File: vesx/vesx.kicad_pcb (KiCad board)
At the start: 4 copper layers, 100 x 40 mm, 181 parts, among them J1 TYPE-C-31-M-12, J2 Conn_01x05, J3 Conn_01x06, J4 Conn_01x03, J5 Conn_01x04, J6 STLINK, J8 CAN, U1 Opamp_Quad, U2 LM1117DT-3.3, U3 LM5164DDA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

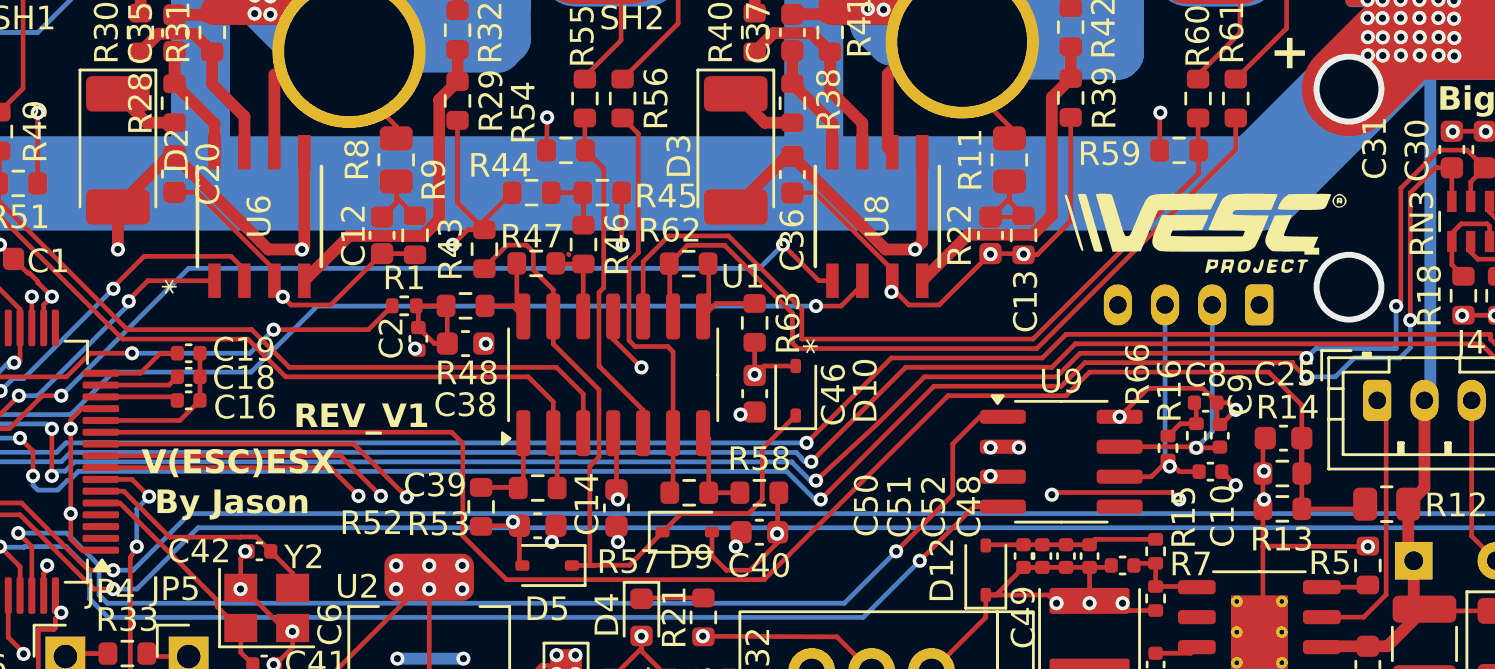
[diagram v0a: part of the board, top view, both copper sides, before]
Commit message: vesc logo del
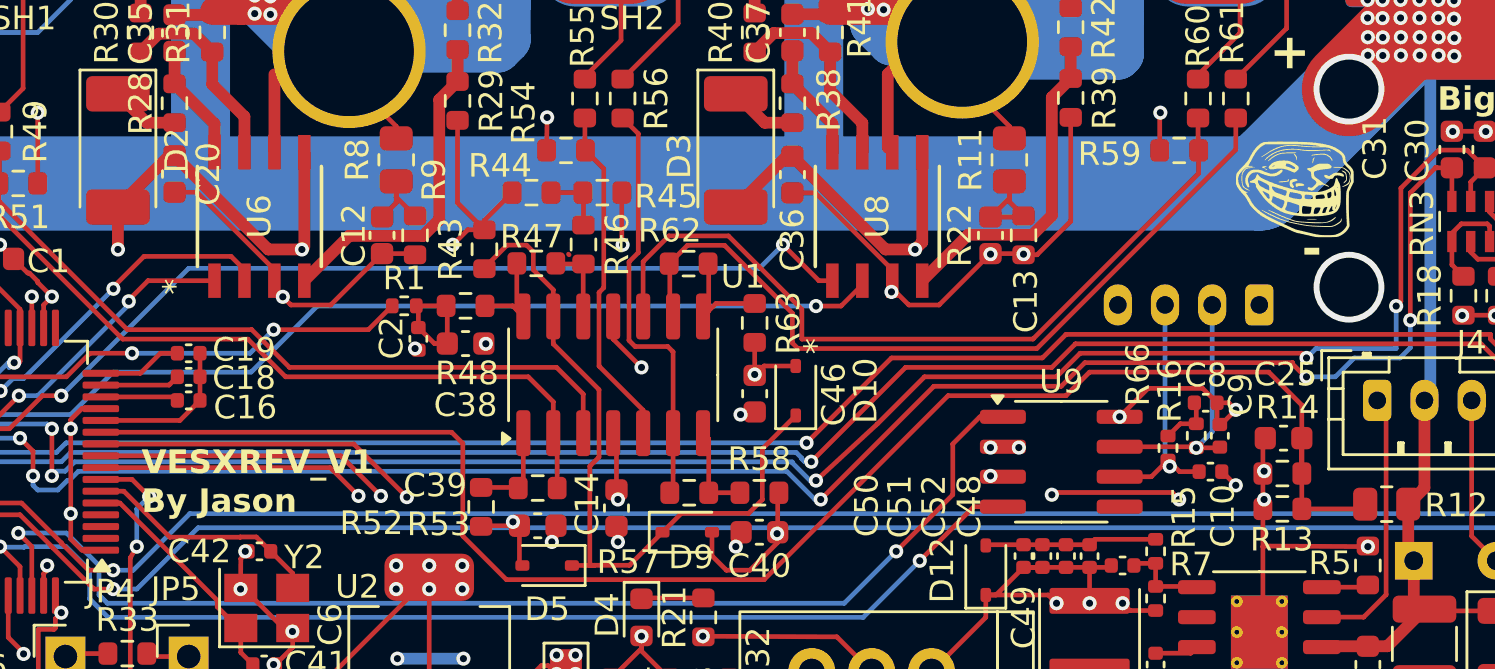
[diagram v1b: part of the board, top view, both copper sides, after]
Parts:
- moved G*** 4.23 mm to (235.7, 28.9)
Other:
- board text added: "VESX"
- board text removed: "V(ESC)ESX"

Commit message: asdf
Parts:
- removed the G*** at (235.7, 28.9)

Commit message: aaaaaaaaaaaaaaaaaaaaaaaaaaaaaaaaaaaaaaaa
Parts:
- C1: footprint Capacitor_SMD:C_0603_1608Metric -> Capacitor_SMD:C_0402_1005Metric
- C24: value 100nF -> 1nF
- C38: value C_Small -> 10nF
- C43: footprint Capacitor_SMD:C_1210_3225Metric -> Capacitor_SMD:C_0603_1608Metric
- L1: footprint Inductor_SMD:L_Abracon_ASPI-4030S -> Inductor_SMD:L_TracoPower_TCK-047_5.2x5.8mm
- R15: footprint Resistor_SMD:R_0402_1005Metric -> Resistor_SMD:R_0603_1608Metric
- moved L1 1.51 mm to (225.5, 47.9)
- moved C43 1.12 mm to (240.5, 49.0)
- moved U4 0.72 mm to (222.1, 51.8)
- moved C1 0.45 mm to (181.0, 32.0)
- moved R15 0.28 mm to (230.0, 44.0)
- renumbered UART2 to J7
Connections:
- net PB11 renamed PB10
- C39 pad 1: CURRENT_A -> CURRENT_C
- C40 pad 1: CURRENT_A -> CURRENT_C
- C46 pad 1: CURRENT_A -> CURRENT_C
- D10 pad 2: CURRENT_A -> CURRENT_C
- D5 pad 2: CURRENT_A -> CURRENT_C
- D9 pad 2: CURRENT_A -> CURRENT_C
- R52 pad 2: CURRENT_A -> CURRENT_C
- R58 pad 2: CURRENT_A -> CURRENT_C
- R63 pad 2: CURRENT_A -> CURRENT_C
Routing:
- net VBAT: track 196.2 -> 197.0 mm
- net GND: track 421.4 -> 421.8 mm, vias 335 -> 333

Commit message: fix trace$ground plane
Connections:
- C39 pad 1: CURRENT_C -> CURRENT_A
- C40 pad 1: CURRENT_C -> CURRENT_B
- D5 pad 2: CURRENT_C -> CURRENT_A
- D9 pad 2: CURRENT_C -> CURRENT_B
- R52 pad 2: CURRENT_C -> CURRENT_A
- R58 pad 2: CURRENT_C -> CURRENT_B
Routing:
- net +3V3: track 378.0 -> 383.4 mm
- net GND: track 421.8 -> 425.4 mm
- net CURRENT_B: track 37.9 -> 37.2 mm

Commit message: eeeeeeeeeeeeeeeeeeee
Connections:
- C39 pad 1: CURRENT_A -> CURRENT_B
- C40 pad 1: CURRENT_B -> CURRENT_C
- D5 pad 2: CURRENT_A -> CURRENT_C
- R52 pad 2: CURRENT_A -> CURRENT_B
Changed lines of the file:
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@@
 			(layers "F.Cu" "F.Paste" "F.Mask")
 			(roundrect_rratio 0.25)
-			(net 48 "CURRENT_B")
+			(net 41 "CURRENT_C")
 			(pintype "passive")
 		)
@@
 			(layers "F.Cu" "F.Paste" "F.Mask")
 			(roundrect_rratio 0.25)
-			(net 34 "CURRENT_A")
+			(net 41 "CURRENT_C")
 			(pinfunction "A")
 			(pintype "passive")
@@
 			(layers "F.Cu" "F.Paste" "F.Mask")
 			(roundrect_rratio 0.25)
-			(net 34 "CURRENT_A")
+			(net 48 "CURRENT_B")
 			(pintype "passive")
 		)
@@
 			(layers "F.Cu" "F.Paste" "F.Mask")
 			(roundrect_rratio 0.25)
-			(net 34 "CURRENT_A")
+			(net 48 "CURRENT_B")
 			(pintype "passive")
 		)
@@
 	)
 	(segment
-		(start 197.925 41.775)
-		(end 195.8 39.65)
+		(start 195.8 39.65)
+		(end 185.075 39.65)
 		(width 0.2)
 		(layer "F.Cu")
@@
 	)
 	(segment
-		(start 213.2 36.34)
-		(end 212.8 36.74)
+		(start 198.05 41.9)
+		(end 195.8 39.65)
 		(width 0.2)
 		(layer "F.Cu")
@@
 	)
 	(segment
-		(start 195.8 39.65)
-		(end 185.075 39.65)
+		(start 213.2 36.34)
+		(end 212.8 36.74)
 		(width 0.2)
 		(layer "F.Cu")
@@
 	)
 	(via
-		(at 197.925 41.775)
+		(at 198.05 41.9)
 		(size 0.6)
 		(drill 0.3)
@@
 	)
 	(segment
-		(start 197.925 41.775)
-		(end 202.7 37)
+		(start 198.05 41.9)
+		(end 202.95 37)
 		(width 0.2)
 		(layer "In2.Cu")
@@
 	)
 	(segment
-		(start 202.7 37)
+		(start 202.95 37)
 		(end 212.5 37)
 		(width 0.2)

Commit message: sav
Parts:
- moved D12 1.00 mm to (221.6, 45.0)
- moved ? 0.50 mm to (254.0, 16.5)
- moved JP4 0.43 mm to (184.0, 48.7)
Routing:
- net GND: track 425.4 -> 356.9 mm, vias 333 -> 331
- net V12V: track 156.4 -> 161.5 mm, vias 8 -> 11
- net +3V3: track 383.4 -> 380.5 mm
- net Net-(U3-SW): track 4.65 -> 6.48 mm
- net MOTOR_TEMP: track 24.6 -> 25.2 mm
- added copper zone on B.Cu, net GND
- added copper zone on F.Cu, net GND
- added copper zone on In2.Cu, net GND

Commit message: drc
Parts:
- moved R29 0.30 mm to (200.5, 25.1)
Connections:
- C39 pad 1: CURRENT_B -> CURRENT_A
- C40 pad 1: CURRENT_C -> CURRENT_B
- D5 pad 2: CURRENT_C -> CURRENT_A
- R52 pad 2: CURRENT_B -> CURRENT_A
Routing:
- net GND: track 356.9 -> 329.6 mm, vias 331 -> 332
- net V5V: track 174.2 -> 187.8 mm
- net +3V3: track 380.5 -> 382.4 mm
- net CURRENT_A: track 22.1 -> 23.8 mm
- net Net-(U8-LVG): track 14.1 -> 15.7 mm
- net CAN_TXD: track 51.1 -> 51.7 mm
- net CAN_RXD: track 48.9 -> 49.5 mm
